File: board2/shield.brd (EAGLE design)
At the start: 66 x 57.8 mm, 41 parts, among them IC1 LM75, J3 22-05-7028-02, J4 WEALTHMETAL DS-214B, J5 22-05-7038-03, K1 G5L, Q1 BC817, U1 LM2596S-5.0

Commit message: Minor changes in PCB design
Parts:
- moved L1 2.01 mm to (21.6, 17.8)
- moved R9 0.64 mm to (21.0, 48.9), turned to 180 degrees
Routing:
- net N$10: track 18.1 -> 10.6 mm
- net LOCK: track 2.23 -> 3.31 mm
- net N$31: track 10.5 -> 11.3 mm

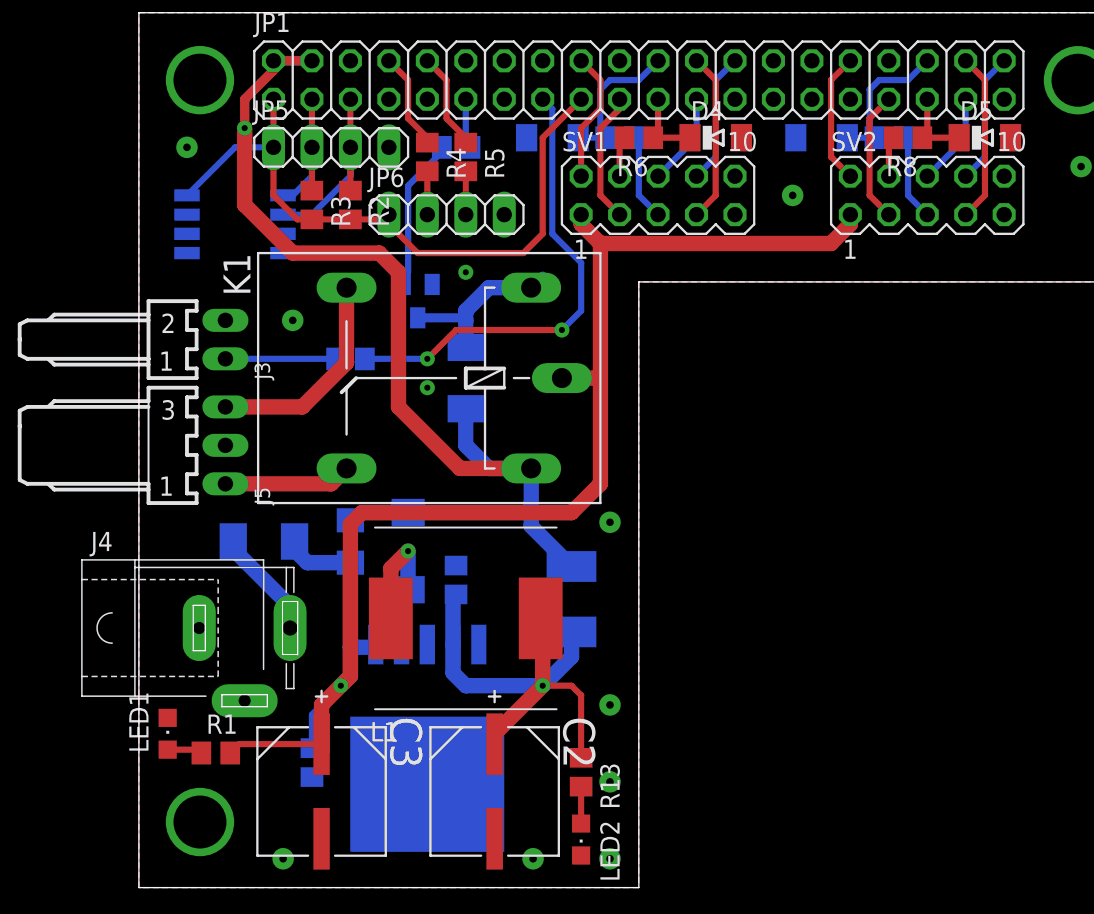
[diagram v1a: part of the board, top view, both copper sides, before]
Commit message: Led added, parts renumbered
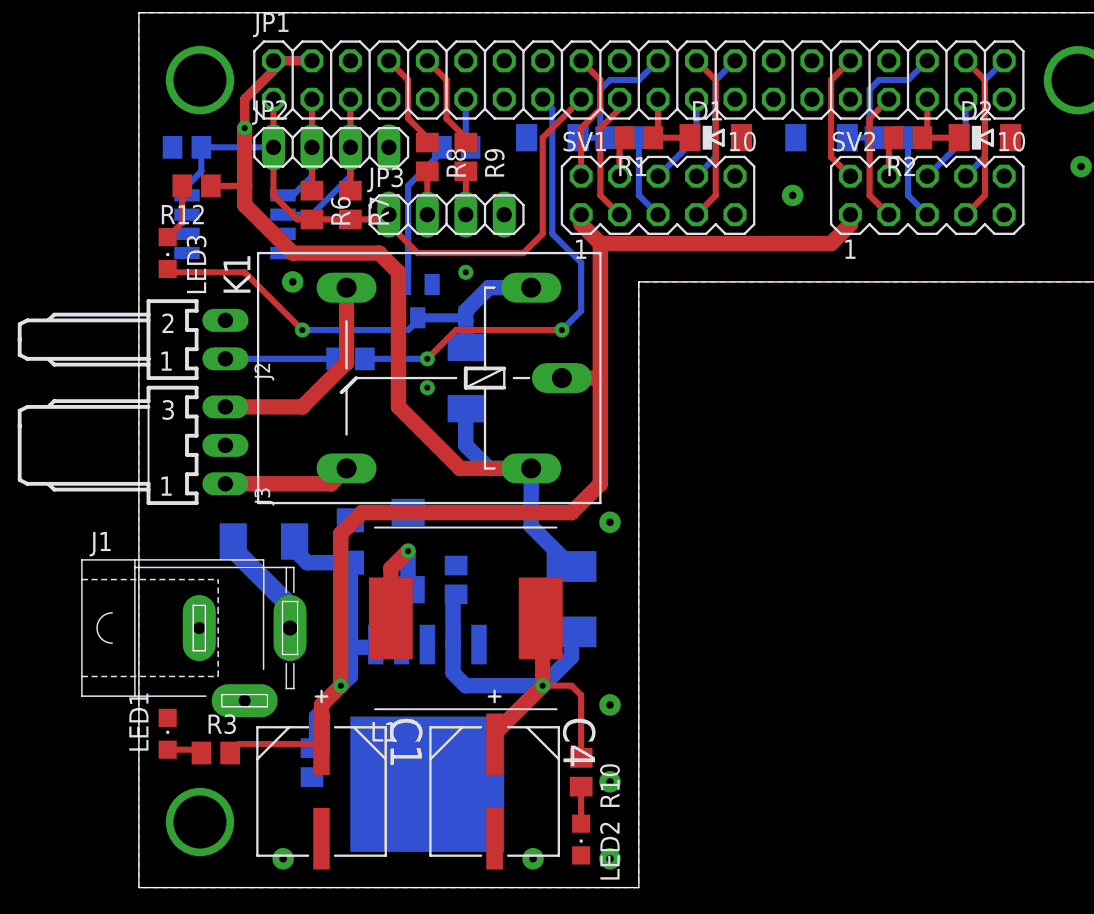
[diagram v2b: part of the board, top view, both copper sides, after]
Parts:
- removed C13: 2.2uF/100V, rcl:C1206
- removed C17: 100n, rcl:C0805
- removed D9: 1N4007 DO-214AC, diode:DO-214AC
- removed J5: 22-05-7038-03, con-molex:7395-03
- added C1: 220UF, Panasonic-EEEFK_EEEFP:CAPAE830X1050N
- added C4: 220u, Panasonic-EEEFK_EEEFP:CAPAE830X1050N
- added C6: 100n, rcl:C0805
- added D1: BZV55C3.0SMD, diode:MINIMELF
- added J2: 22-05-7028-02, con-molex:7395-02
- added LED3: SML-LX0805SUGC-TR, led:CHIPLED_0805
- added R12: 560R, rcl:R0805
- C2: value 220UF -> 100n; device Panasonic-EEEFK_EEEFP:CAPAE830X1050N -> rcl:C0805
- C3: value 220UF -> 2.2uF/100V; device Panasonic-EEEFK_EEEFP:CAPAE830X1050N -> rcl:C1206
- D2: value 1N4007 DO-214AC -> BZV55C3.0SMD; device diode:DO-214AC -> diode:MINIMELF
- D3: value SSB44-E3/52T -> 1N4007 DO-214AC; device diode:DO214AA -> diode:DO-214AC
- D6: value BZV55C3.0SMD -> SSB44-E3/52T; device diode:MINIMELF -> diode:DO214AA
- D7: value BZV55C3.0SMD -> 1N4007 DO-214AC; device diode:MINIMELF -> diode:DO-214AC
- F1: value 1812L -> PPTC1812SMD110/16V
- J3: value 22-05-7028-02 -> 22-05-7038-03; device con-molex:7395-02 -> con-molex:7395-03
- R1: value 5K6 -> 1k7
- R10: value 1k7 -> 560R
- R11: value 1k7 -> 1k
- R13: value 560R -> 860R
- R2: value 4k7 -> 1k7
- R3: value 4k7 -> 5K6
- R4, R5: value 120R -> 1k7
- R6: value 1k7 -> 4k7
- R7: value 1k -> 4k7
- R8: value 1k7 -> 120R
- R9: value 1k5 -> 120R
- moved R1 49.3 mm to (33.0, 49.5), turned to 180 degrees
- moved R13 42.1 mm to (21.0, 48.9), flipped to the bottom, turned to 180 degrees
- moved R10 42.0 mm to (29.2, 7.62), flipped to the top, turned to 270 degrees
- moved R11 38.4 mm to (14.0, 34.9), turned to 180 degrees
- moved D2 37.8 mm to (55.9, 49.5), flipped to the top, turned to 0 degrees
- moved R2 37.1 mm to (50.8, 49.5), turned to 180 degrees
- moved R3 36.7 mm to (5.08, 8.89), turned to 0 degrees
- moved R8 31.8 mm to (19.1, 48.3), turned to 270 degrees
- moved D6 28.9 mm to (17.8, 22.2), turned to 90 degrees
- moved D7 28.4 mm to (21.6, 33.7), turned to 90 degrees
- moved R5 28.0 mm to (49.5, 49.5), flipped to the bottom, turned to 0 degrees
- moved R6 22.0 mm to (11.4, 45.1), turned to 270 degrees
- moved C3 16.6 mm to (14.0, 22.9), flipped to the bottom, turned to 90 degrees
- moved C5 15.4 mm to (21.0, 20.3), turned to 270 degrees
- moved R4 12.8 mm to (31.8, 49.5), flipped to the bottom, turned to 0 degrees
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- renumbered J4 to J1, JP5 to JP2, JP6 to JP3, Q1 to T1
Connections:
- removed net N$9: D9.A, J1.3
- new net N$11: LED3.A, R12.2
- new net UIN: D3.A, J1.3
- net +24V: now also C1.1, C2.2, D3.C, R3.2; no longer C13.1, C5.2, D9.C, R1.2
- net +3V3: now also C6.2, R6.2, R7.2; no longer R2.2, R3.2
- net +5V: now also D7.C, R12.1; no longer D2.C
- net GND: now also C1.2, C2.1, C4.2, C6.1, D1.A, D2.A, J2.2; no longer C13.2, C17.1, C2.2, D3.A, D7.A, J5.2
- net I-D0: now also R1.2; no longer R6.2
- net I-D0-3V3: now also D1.C, R1.1; no longer D4.C, R6.1
- net I-D1: now also R4.1; no longer R10.1
- net I-D1-3V3: now also D4.C, R4.2; no longer D6.C, R10.2
- net LOCK: now also R13.2; no longer R9.2
- net N$1: now also C4.1, C5.2, R10.1; no longer C17.2, C2.1, R13.1
- net N$10: now also R13.1; no longer R9.1
- net N$2: now also J2.1, R11.1; no longer J3.1, R7.1
- net N$23: now also R3.1; no longer R1.1
- net N$3: now also R8.2; no longer R4.2
- net N$31: now also D6.C; no longer D3.C
- net N$4: now also R10.2; no longer R13.2
- net N$5: now also J3.3; no longer J5.3
- net N$6: now also R9.2; no longer R5.2
- net N$7: now also J3.1; no longer J5.1
- net N$8: now also D7.A, LED3.C; no longer D2.A
- net O-D0: now also R2.2; no longer R8.2
- net O-D0-3V3: now also D2.C, R2.1; no longer D5.C, R8.1
- net O-D1: now also R5.1; no longer R11.1
- net O-D1-3V3: now also D5.C, R5.2; no longer D7.C, R11.2
- net RXD: now also R9.1; no longer R5.1
- net SCL: now also R7.1; no longer R2.1
- net SDA: now also R6.1; no longer R3.1
- net TAMPER: now also R11.2; no longer R7.2
- net TXD: now also R8.1; no longer R4.1
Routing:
- net N$8: track 11.7 -> 29.2 mm, vias 0 -> 1
- net UIN: track 0.00 -> 7.27 mm
- net N$9: track 7.27 -> 0.00 mm
- net N$11: track 0.00 -> 3.79 mm
- net +5V: track 66.9 -> 69.1 mm
- net +3V3: track 43.8 -> 45.1 mm

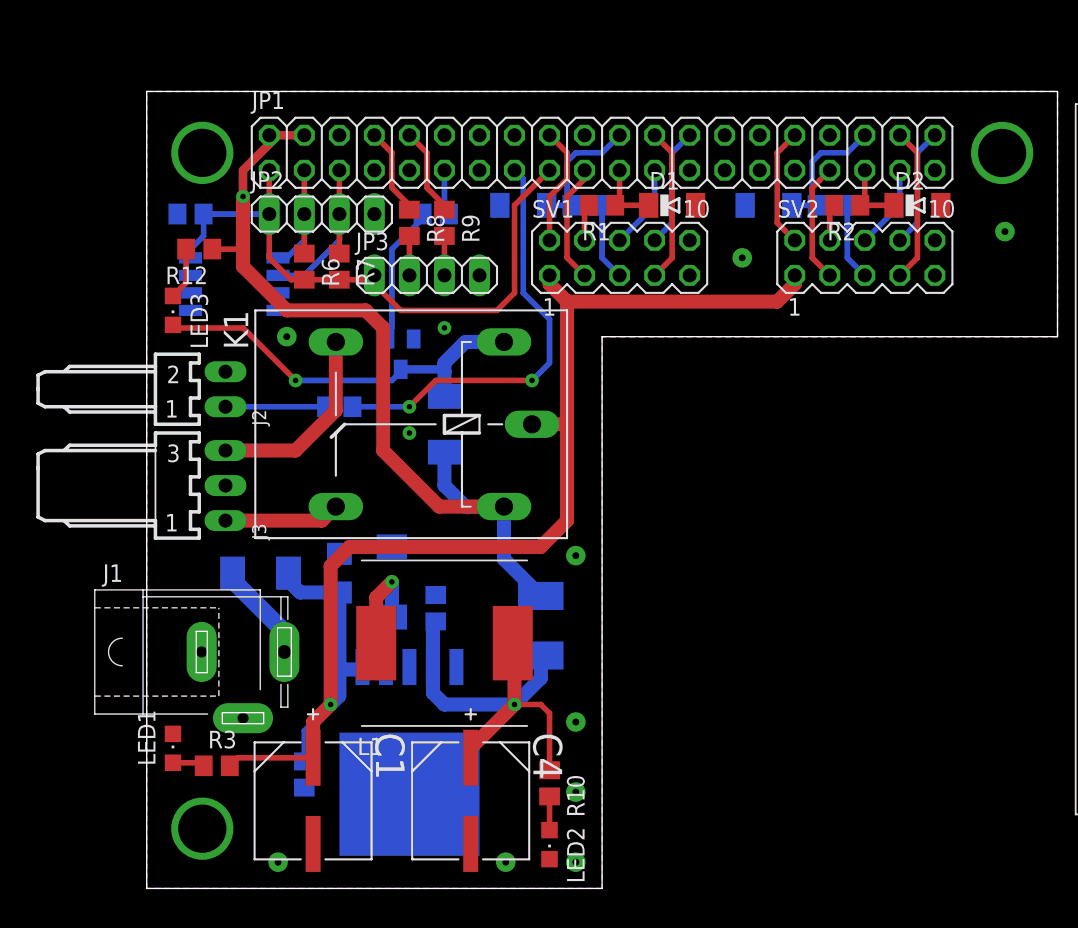
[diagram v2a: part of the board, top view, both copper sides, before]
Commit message: Names reordered
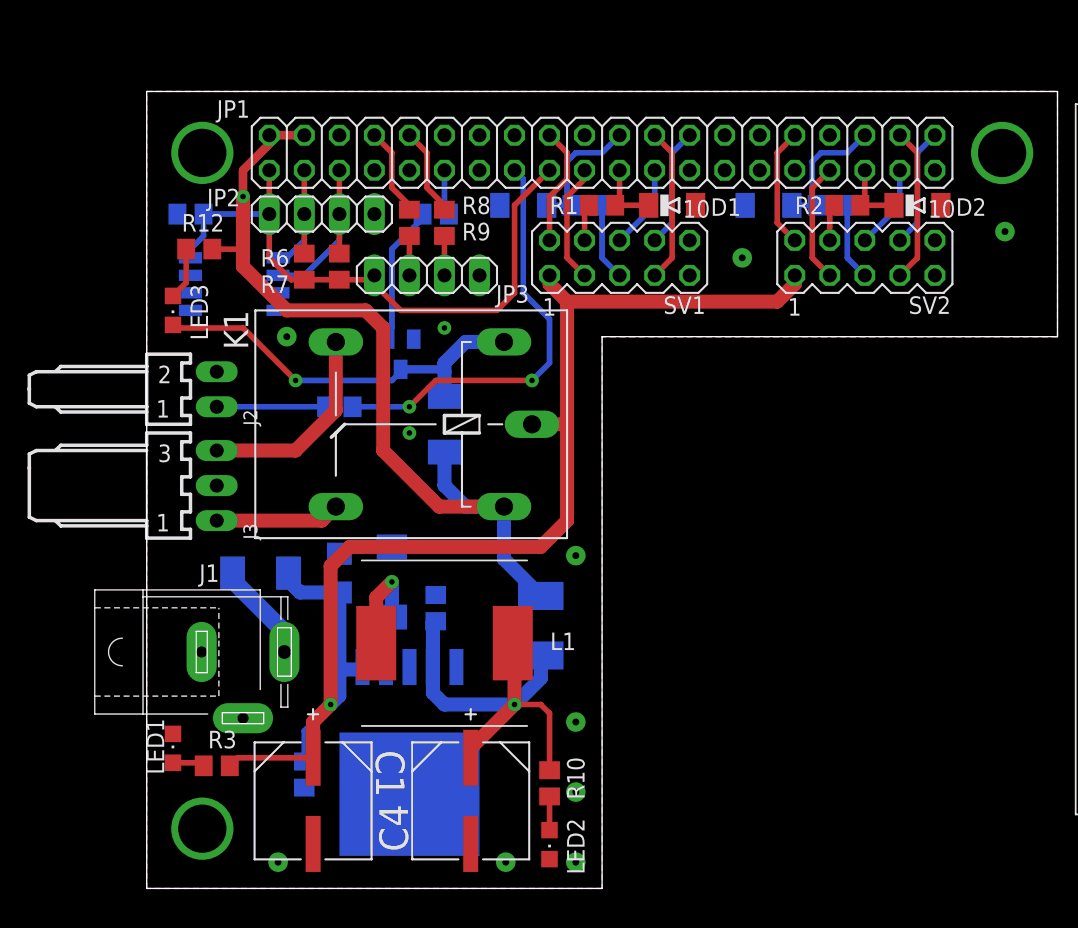
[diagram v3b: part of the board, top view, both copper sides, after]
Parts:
- moved J2 0.63 mm to (5.08, 36.2)
- moved J3 0.63 mm to (5.08, 29.2)
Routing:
- net N$7: track 8.42 -> 9.06 mm
- net N$2: track 7.30 -> 7.94 mm
- net N$5: track 14.2 -> 14.8 mm
